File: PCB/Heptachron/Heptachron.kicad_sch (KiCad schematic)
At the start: 1 part, among them U1 BQ24230RGT

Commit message: More PCB work
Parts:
- added C1, C4: 100n, symbol Device:C_Small
- added C2, C3, C5: 4.7u, symbol Device:C_Small
- added R1, R2, R3, R4, R8: 10K, symbol Device:R_Small
- added R5: 3.3K, symbol Device:R_Small
- added R6: 4.7K, symbol Device:R_Small
- added R7: DNP, symbol Device:R_Small
- added SW1, SW2: SW_Push, symbol Switch:SW_Push
- added U2: ATtiny424-SS, Package_SO:SOIC-14_3.9x8.7mm_P1.27mm, symbol MCU_Microchip_ATtiny:ATtiny424-SS
- added U3: IS31FL3729, Package_QFP:TQFP-32_7x7mm_P0.8mm, symbol Heptachron:IS32FL3729
- added X1: RV-3028-C7, Heptachron-Lib:RV-3028-C7, symbol Heptachron:RV-3028-C7
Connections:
- net at U1.1 (TS): now also R8.2
- net VCC: now reaches U1.10 (OUT), U1.11 (OUT)
- net VCC: now also U1.5 (EN2), C1.2, C2.2, C4.2, R3.1, R4.2, U2.1 (VCC), X1.7 (VDD)
- net at U1.12 (ILIM): now also R5.2
- net +5V: now reaches U1.13 (IN)
- net +5V: now also C5.1
- net at U1.15 (TD): now also R7.1
- net at U1.16 (ISET): now also R6.2
- net GND: now reaches U1.17 (VSS), U1.8 (VSS)
- net GND: now also U1.4 (CE), U1.6 (EN1), C1.1, C2.1, C3.1, C4.1, C5.2, R1.1, R2.1, R5.1, R6.1, R7.2, R8.1, U2.14 (GND), U3.24 (GND), U3.28 (AD), U3.9 (GND), X1.5 (VSS)
- net +BATT: now reaches U1.2 (BAT), U1.3 (BAT)
- net +BATT: now also C3.2
- net PGOOD: now reaches U1.7 (PGOOD)
- net PGOOD: now also R3.2
- net CHG: now reaches U1.9 (CHG)
- net CHG: now also R4.1
- new net: R1.2, X1.6 (VBU)
- new net: R2.2, X1.8 (EVI)
- new net RTC_CLK: U2.6 (PB3), X1.1 (CLKOUT)
- new net SCL: U2.9 (PB0), U3.27 (SCL), X1.3 (SCL)
- new net SDA: U2.8 (PB1), U3.26 (SDA), X1.4 (SDA)
- new net UPDI: U2.10 (~{RESET}/PA0)
- no-connect marks 0 -> 2
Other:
- note added: "=ITERM"
- note added: "ADDR: 0x34"
- note added: "ADDR: 0x52"
- note added: "Advanced power management possible, including backup power"
- note added: "R_ISET = 870/I_CHG R_ILIM = 1530/I_MAX"

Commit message: LEDs and more
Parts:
- added D1, D2, D3, D4, D5, D6, D7: CLM, Heptachron-Lib:CREE-PLCC2-custom, symbol Device:LED_Small
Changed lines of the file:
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@@
+    )
+  )
+  (symbol (lib_id "Device:LED_Small") (at 165.1 111.76 90) (unit 1)
+    (in_bom yes) (on_board yes) (dnp no) (fields_autoplaced)
+    (property "Reference" "D5" (at 167.64 110.4265 90)
+      (effects (font (size 1.27 1.27)) (justify right))
+    )
+    (property "Value" "CLM" (at 167.64 112.9665 90)
+      (effects (font (size 1.27 1.27)) (justify right))
+    )
+    (property "Footprint" "Heptachron-Lib:CREE-PLCC2-custom" (at 165.1 111.76 90)
+      (effects (font (size 1.27 1.27)) hide)
+    )
+    (property "Datasheet" "~" (at 165.1 111.76 90)
+      (effects (font (size 1.27 1.27)) hide)
+    )
+    (pin "1")
+    (pin "2")
+    (instances
+      (project "Heptachron"
+        (path "/c6ec4407-9aab-4aab-950a-5d337d47ac64"
+          (reference "D5") (unit 1)
+        )
+      )
     )
   )
@@
         (path "/c6ec4407-9aab-4aab-950a-5d337d47ac64"
           (reference "SW2") (unit 1)
+        )
+      )
+    )
+  )
+  (symbol (lib_id "Device:LED_Small") (at 184.15 111.76 90) (unit 1)
+    (in_bom yes) (on_board yes) (dnp no) (fields_autoplaced)
+    (property "Reference" "D6" (at 186.69 110.4265 90)
+      (effects (font (size 1.27 1.27)) (justify right))
+    )
+    (property "Value" "CLM" (at 186.69 112.9665 90)
+      (effects (font (size 1.27 1.27)) (justify right))
+    )
+    (property "Footprint" "Heptachron-Lib:CREE-PLCC2-custom" (at 184.15 111.76 90)
+      (effects (font (size 1.27 1.27)) hide)
+    )
+    (property "Datasheet" "~" (at 184.15 111.76 90)
+      (effects (font (size 1.27 1.27)) hide)
+    )
+    (pin "1")
+    (pin "2")
+    (instances
+      (project "Heptachron"
+        (path "/c6ec4407-9aab-4aab-950a-5d337d47ac64"
+          (reference "D6") (unit 1)
         )
       )
@@
     )
   )
+  (symbol (lib_id "Device:LED_Small") (at 175.26 83.82 90) (unit 1)
+    (in_bom yes) (on_board yes) (dnp no) (fields_autoplaced)
+    (property "Reference" "D1" (at 177.8 82.4865 90)
+      (effects (font (size 1.27 1.27)) (justify right))
+    )
+    (property "Value" "CLM" (at 177.8 85.0265 90)
+      (effects (font (size 1.27 1.27)) (justify right))
+    )
+    (property "Footprint" "Heptachron-Lib:CREE-PLCC2-custom" (at 175.26 83.82 90)
+      (effects (font (size 1.27 1.27)) hide)
+    )
+    (property "Datasheet" "~" (at 175.26 83.82 90)
+      (effects (font (size 1.27 1.27)) hide)
+    )
+    (pin "1")
+    (pin "2")
+    (instances
+      (project "Heptachron"
+        (path "/c6ec4407-9aab-4aab-950a-5d337d47ac64"
+          (reference "D1") (unit 1)
+        )
+      )
+    )
+  )
   (symbol (lib_id "Device:C_Small") (at 50.8 96.52 90) (mirror x) (unit 1)
     (in_bom yes) (on_board yes) (dnp no) (fields_autoplaced)
@@
         (path "/c6ec4407-9aab-4aab-950a-5d337d47ac64"
           (reference "SW1") (unit 1)
+        )
+      )
+    )
+  )
+  (symbol (lib_id "Device:LED_Small") (at 175.26 101.6 90) (unit 1)
+    (in_bom yes) (on_board yes) (dnp no) (fields_autoplaced)
+    (property "Reference" "D4" (at 177.8 100.2665 90)
+      (effects (font (size 1.27 1.27)) (justify right))
+    )
+    (property "Value" "CLM" (at 177.8 102.8065 90)
+      (effects (font (size 1.27 1.27)) (justify right))
+    )
+    (property "Footprint" "Heptachron-Lib:CREE-PLCC2-custom" (at 175.26 101.6 90)
+      (effects (font (size 1.27 1.27)) hide)
+    )
+    (property "Datasheet" "~" (at 175.26 101.6 90)
+      (effects (font (size 1.27 1.27)) hide)
+    )
+    (pin "1")
+    (pin "2")
+    (instances
+      (project "Heptachron"
+        (path "/c6ec4407-9aab-4aab-950a-5d337d47ac64"
+          (reference "D4") (unit 1)
         )
       )
@@
     )
   )
+  (symbol (lib_id "Device:LED_Small") (at 175.26 120.65 90) (unit 1)
+    (in_bom yes) (on_board yes) (dnp no) (fields_autoplaced)
+    (property "Reference" "D7" (at 177.8 119.3165 90)
+      (effects (font (size 1.27 1.27)) (justify right))
+    )
+    (property "Value" "CLM" (at 177.8 121.8565 90)
+      (effects (font (size 1.27 1.27)) (justify right))
+    )
+    (property "Footprint" "Heptachron-Lib:CREE-PLCC2-custom" (at 175.26 120.65 90)
+      (effects (font (size 1.27 1.27)) hide)
+    )
+    (property "Datasheet" "~" (at 175.26 120.65 90)
+      (effects (font (size 1.27 1.27)) hide)
+    )
+    (pin "1")
+    (pin "2")
+    (instances
+      (project "Heptachron"
+        (path "/c6ec4407-9aab-4aab-950a-5d337d47ac64"
+          (reference "D7") (unit 1)
+        )
+      )
+    )
+  )
   (symbol (lib_id "Device:R_Small") (at 67.31 46.99 0) (unit 1)
     (in_bom yes) (on_board yes) (dnp no)
@@
         (path "/c6ec4407-9aab-4aab-950a-5d337d47ac64"
           (reference "R3") (unit 1)
+        )
+      )
+    )
+  )
+  (symbol (lib_id "Device:LED_Small") (at 184.15 92.71 90) (unit 1)
+    (in_bom yes) (on_board yes) (dnp no) (fields_autoplaced)
+    (property "Reference" "D3" (at 186.69 91.3765 90)
+      (effects (font (size 1.27 1.27)) (justify right))
+    )
+    (property "Value" "CLM" (at 186.69 93.9165 90)
+      (effects (font (size 1.27 1.27)) (justify right))
+    )
+    (property "Footprint" "Heptachron-Lib:CREE-PLCC2-custom" (at 184.15 92.71 90)
+      (effects (font (size 1.27 1.27)) hide)
+    )
+    (property "Datasheet" "~" (at 184.15 92.71 90)
+      (effects (font (size 1.27 1.27)) hide)
+    )
+    (pin "1")
+    (pin "2")
+    (instances
+      (project "Heptachron"
+        (path "/c6ec4407-9aab-4aab-950a-5d337d47ac64"
+          (reference "D3") (unit 1)
         )
       )
@@
         )
       )
+    )
+  )
+  (symbol (lib_id "Device:LED_Small") (at 166.37 92.71 90) (unit 1)
+    (in_bom yes) (on_board yes) (dnp no) (fields_autoplaced)
+    (property "Reference" "D2" (at 168.91 91.3765 90)
+      (effects (font (size 1.27 1.27)) (justify right))
+    )
+    (property "Value" "CLM" (at 168.91 93.9165 90)
+      (effects (font (size 1.27 1.27)) (justify right))
+    )
+    (property "Footprint" "Heptachron-Lib:CREE-PLCC2-custom" (at 166.37 92.71 90)
+      (effects (font (size 1.27 1.27)) hide)
+    )
+    (property "Datasheet" "~" (at 166.37 92.71 90)
+      (effects (font (size 1.27 1.27)) hide)
+    )
+    (pin "1")
+    (pin "2")
+    (instances
+      (project "Heptachron"
+        (path "/c6ec4407-9aab-4aab-950a-5d337d47ac64"
+          (reference "D2") (unit 1)
+        )
+      )

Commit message: Continue schematic
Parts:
- added D36, D37: CLM, LED_SMD:LED_0603_1608Metric, symbol Device:LED_Small
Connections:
- net CS4: now reaches U3.1 (CS4)
- net SW8: now reaches U3.15 (SW8)
- net SW7: now reaches U3.16 (SW7)
- net SW6: now reaches U3.17 (SW6)
- net SW5: now reaches U3.18 (SW5)
- net SW4: now reaches U3.19 (SW4)
- net CS5: now reaches U3.2 (CS5)
- net SW3: now reaches U3.20 (SW3)
- net SW2: now reaches U3.21 (SW2)
- net SW1: now reaches U3.22 (SW1)
- net CS6: now reaches U3.3 (CS6)
- net CS1: now reaches U3.30 (CS1)
- net CS2: now reaches U3.31 (CS2)
- net CS3: now reaches U3.32 (CS3)
- net CS7: now reaches U3.4 (CS7)
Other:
- added sheet 7-Segment-Cree-PLCC2 (7-Segment-Cree-PLCC2.kicad_sch)
- added sheet 7-Segment-Cree-PLCC3 (7-Segment-Cree-PLCC2.kicad_sch)
- added sheet 7-Segment-Cree-PLCC4 (7-Segment-Cree-PLCC2.kicad_sch)
- added sheet 7-Segment-Cree-PLCC5 (7-Segment-Cree-PLCC2.kicad_sch)
- note added: "CS:n - Current sink 'n', one for each digit [CATHODE] SW:n - Switch power source, one for each segment [ANODE] SW1: A, SW2: B, ..., SW7: G ◄ A F ▲ ▼ B ◄ G E ▲ ▼ C ◄ D"
- note added: "Colon"
- note added: "Digit 1 CS1 SW 1:7 ─── │ │ │ │ ─── │ │ │ │ ───"
- note added: "Digit 2 CS2 SW 1:7 ─── │ │ │ │ ─── │ │ │ │ ───"
- note added: "Digit 3 CS3 SW 1:7 ─── │ │ │ │ ─── │ │ │ │ ───"
- note added: "Digit 4 CS4 SW 1:7 ─── │ │ │ │ ─── │ │ │ │ ───"
- note added: "│ │"
- moved on the sheet: D1, D2, D3, D4, D5, D6, D7

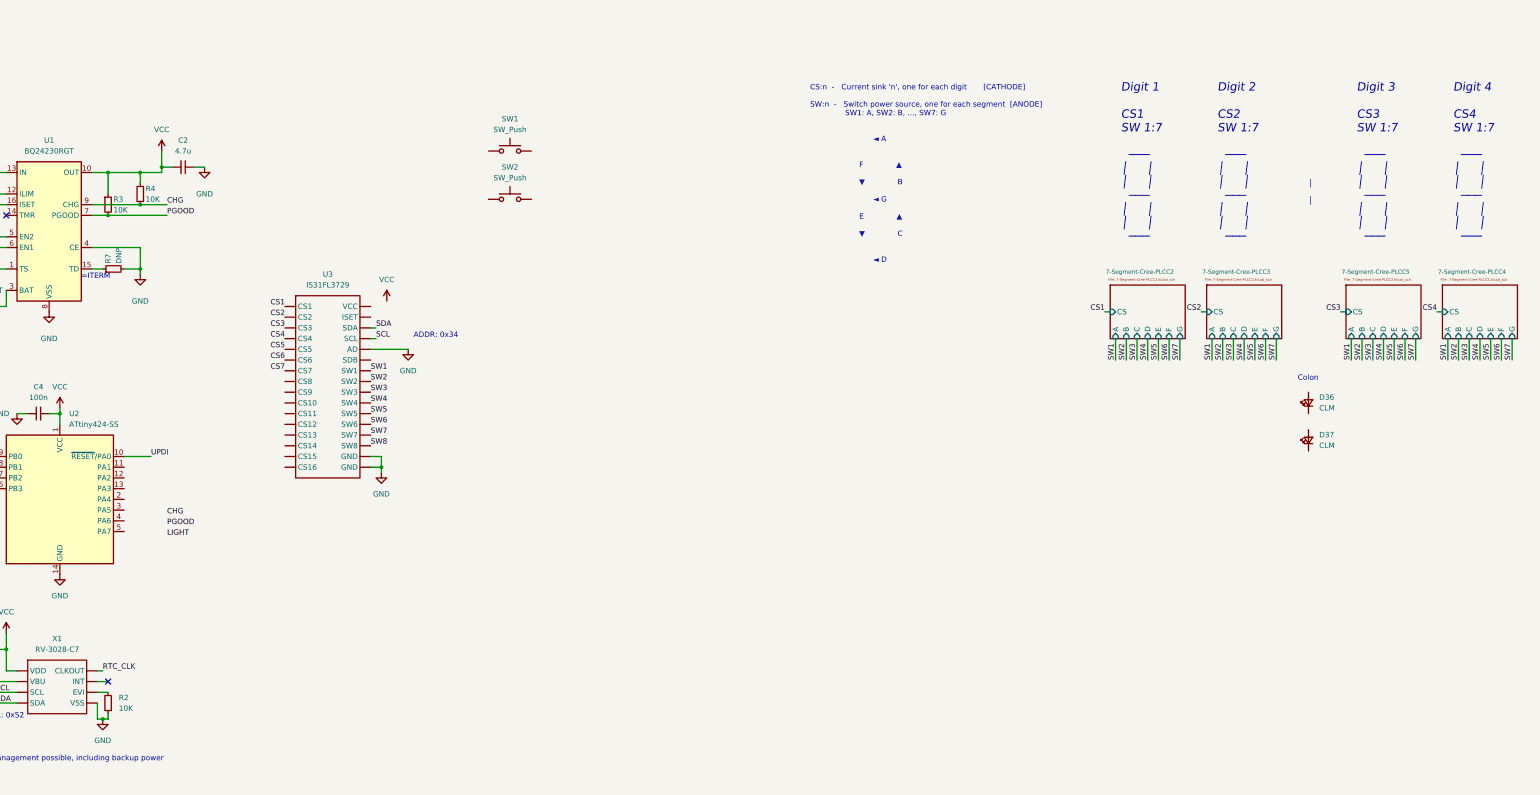
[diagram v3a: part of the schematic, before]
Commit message: Continue schematic, symbols & footprints for digits
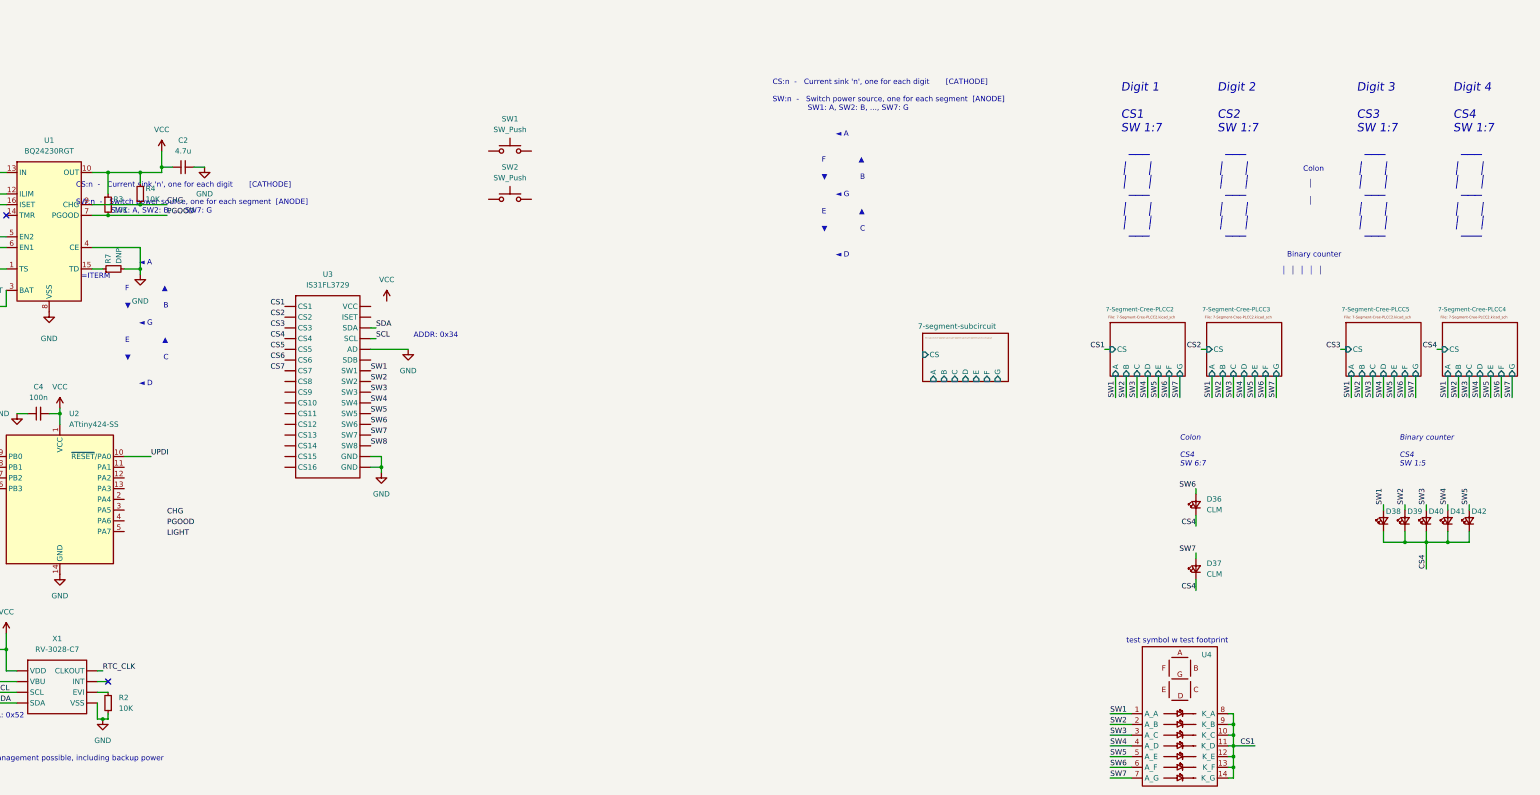
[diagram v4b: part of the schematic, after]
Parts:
- added D38, D39, D40, D41, D42: ~, LED_SMD:LED_0603_1608Metric, symbol Device:LED_Small
- added U4: ~, Heptachron-Lib:7-segment-digit-Cree, symbol Heptachron:7-segment-digit
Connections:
- net CS1: now also U4.10 (K_C), U4.11 (K_D), U4.12 (K_E), U4.13 (K_F), U4.14 (K_G), U4.8 (K_A), U4.9 (K_B)
- net CS4: now also D36.1 (K), D37.1 (K), D38.1 (K), D39.1 (K), D40.1 (K), D41.1 (K), D42.1 (K)
- net SW1: now also D38.2 (A), U4.1 (A_A)
- net SW2: now also D39.2 (A), U4.2 (A_B)
- net SW3: now also D40.2 (A), U4.3 (A_C)
- net SW4: now also D41.2 (A), U4.4 (A_D)
- net SW5: now also D42.2 (A), U4.5 (A_E)
- net SW6: now also D36.2 (A), U4.6 (A_F)
- net SW7: now also D37.2 (A), U4.7 (A_G)
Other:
- added sheet 7-segment-subcircuit (Sub-circuits/7-segment-subcircuit/7-segment-subcircuit/7-segment-subcircuit.kicad_sch)
- note added: "Binary counter"
- note added: "Binary counter CS4 SW 1:5"
- note added: "Colon CS4 SW 6:7"
- note added: "test symbol w test footprint"
- note added: "│ │ │ │ │"
- moved on the sheet: D36, D37

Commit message: PCB work and 3D modeling
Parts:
- added U2, U3, U4: ~, Heptachron-Lib:7-segment-digit-Cree, symbol Heptachron:7-segment-digit
- renumbered U4 to U1, U1 to U6, U3 to U7, U2 to U8
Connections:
- net CS2: now also U2.10 (K_C), U2.11 (K_D), U2.12 (K_E), U2.13 (K_F), U2.14 (K_G), U2.8 (K_A), U2.9 (K_B)
- net CS3: now also U3.10 (K_C), U3.11 (K_D), U3.12 (K_E), U3.13 (K_F), U3.14 (K_G), U3.8 (K_A), U3.9 (K_B)
- net CS4: now also U4.10 (K_C), U4.11 (K_D), U4.12 (K_E), U4.13 (K_F), U4.14 (K_G), U4.8 (K_A), U4.9 (K_B)
- net SW1: now also U2.1 (A_A), U3.1 (A_A), U4.1 (A_A)
- net SW2: now also U2.2 (A_B), U3.2 (A_B), U4.2 (A_B)
- net SW3: now also U2.3 (A_C), U3.3 (A_C), U4.3 (A_C)
- net SW4: now also U2.4 (A_D), U3.4 (A_D), U4.4 (A_D)
- net SW5: now also U2.5 (A_E), U3.5 (A_E), U4.5 (A_E)
- net SW6: now also U2.6 (A_F), U3.6 (A_F), U4.6 (A_F)
- net SW7: now also U2.7 (A_G), U3.7 (A_G), U4.7 (A_G)
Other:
- note added: "old disgusting stuff"
- note removed: "test symbol w test footprint"
- moved on the sheet: D36, D37, D38, D39, D40, D41, D42, U1
